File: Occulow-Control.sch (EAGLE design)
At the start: 41 parts, among them T1 DMP3010LK3, T2 DMP3010LK3, T3 DMP3010LK3

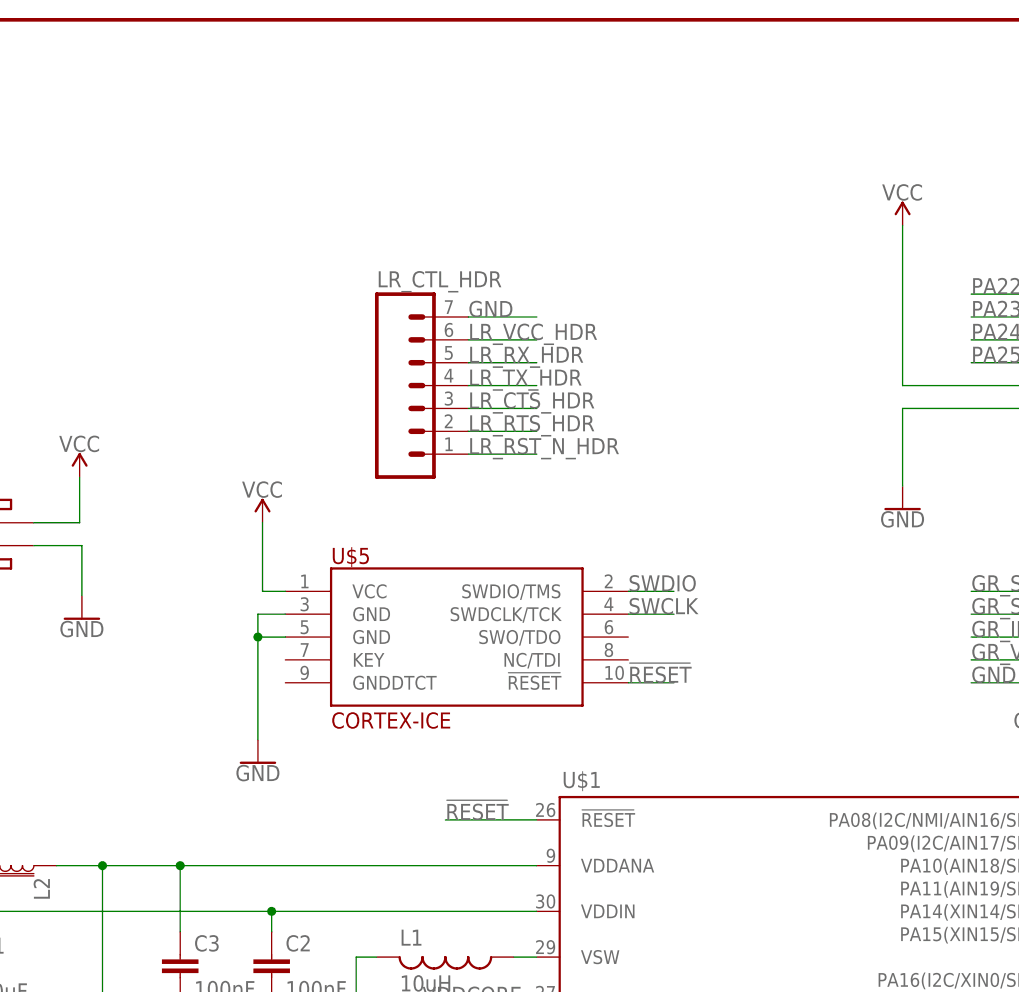
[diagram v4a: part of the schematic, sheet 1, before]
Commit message: Added vcc pull up for reset and button switch. Fixes #7
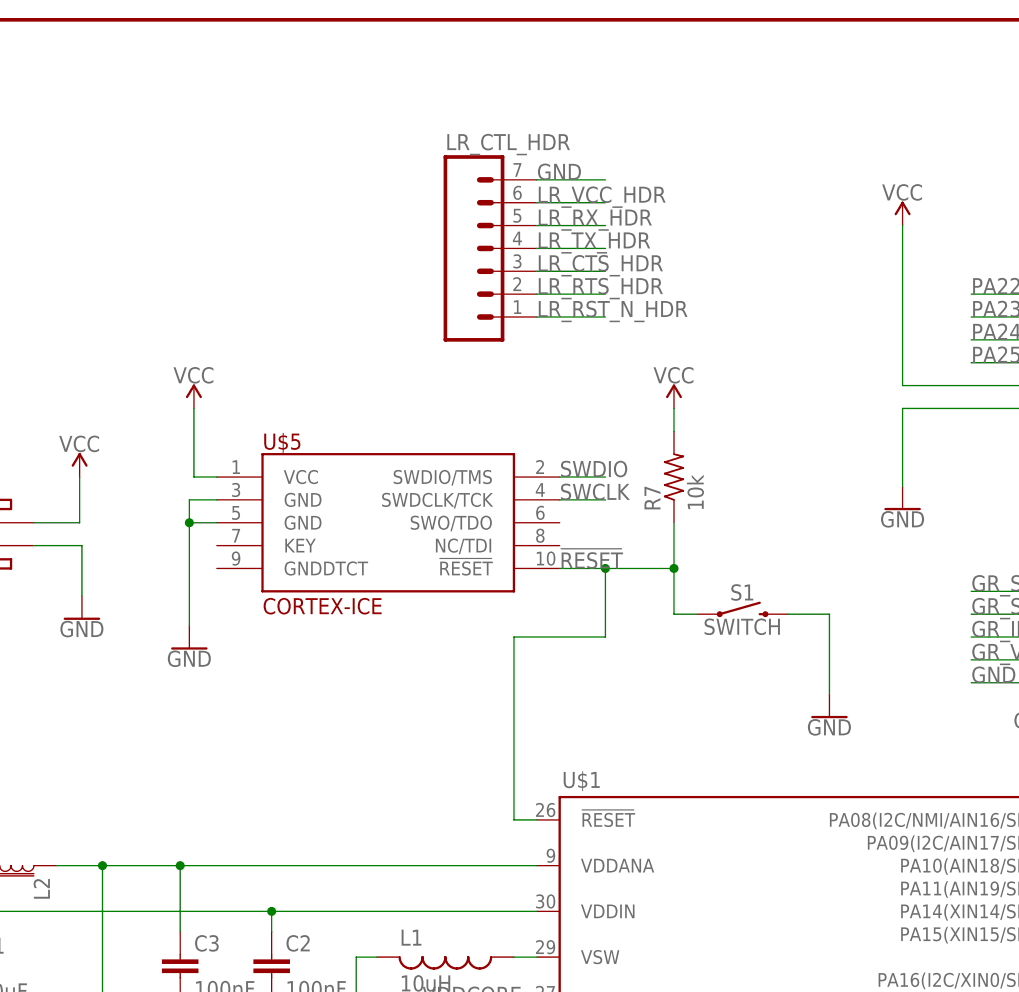
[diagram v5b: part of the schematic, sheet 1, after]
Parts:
- added R7: 10k, resistor:R-US_R1206
- added S1: SWITCH, SparkFun-Switches:MOMENTARY-SWITCH-SPST-SMD-5.2-REDUNDANT
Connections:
- net !RESET: now also R7.1, S1.1
- net GND: now also S1.2
- net VCC: now also R7.2
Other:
- moved on the sheet: LR_CTL_HDR, U$5
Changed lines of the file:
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@@
 <part name="R6" library="resistor" deviceset="R-US_" device="R1206" value="330"/>
 <part name="GND5" library="SparkFun-PowerSymbols" deviceset="GND" device=""/>
+<part name="S1" library="SparkFun-Switches" deviceset="MOMENTARY-SWITCH-SPST" device="-SMD-5.2-REDUNDANT" value="SWITCH"/>
+<part name="R7" library="resistor" deviceset="R-US_" device="R1206" value="10k"/>
+<part name="SUPPLY2" library="SparkFun-PowerSymbols" deviceset="VCC" device=""/>
+<part name="GND6" library="SparkFun-PowerSymbols" deviceset="GND" device=""/>
 </parts>
 <sheets>
@@
 <instance part="T3" gate="G$1" x="226.822" y="134.62"/>
 <instance part="R1" gate="G$1" x="165.1" y="53.34" rot="R90"/>
-<instance part="SUPPLY4" gate="G$1" x="45.72" y="129.54"/>
-<instance part="GND9" gate="1" x="45.212" y="102.87"/>
+<instance part="SUPPLY4" gate="G$1" x="38.1" y="142.24"/>
+<instance part="GND9" gate="1" x="37.592" y="115.57"/>
 <instance part="SUPPLY5" gate="G$1" x="116.84" y="162.56"/>
 <instance part="GND10" gate="1" x="116.84" y="131.064"/>
@@
 <instance part="H2" gate="G$1" x="40.64" y="5.08"/>
 <instance part="H3" gate="G$1" x="45.72" y="5.08"/>
-<instance part="LR_CTL_HDR" gate="G$1" x="63.5" y="142.24"/>
-<instance part="U$5" gate="G$1" x="66.04" y="116.84"/>
+<instance part="LR_CTL_HDR" gate="G$1" x="71.12" y="157.48"/>
+<instance part="U$5" gate="G$1" x="58.42" y="129.54"/>
 <instance part="D1" gate="G$1" x="195.58" y="68.58"/>
 <instance part="R6" gate="G$1" x="195.58" y="55.88" rot="R90"/>
 <instance part="GND5" gate="1" x="195.58" y="43.18"/>
+<instance part="S1" gate="G$1" x="99.06" y="119.38"/>
+<instance part="R7" gate="G$1" x="91.44" y="134.62" rot="R90"/>
+<instance part="SUPPLY2" gate="G$1" x="91.44" y="142.24"/>
+<instance part="GND6" gate="1" x="108.712" y="107.95"/>
 </instances>
 <busses>
@@
 <segment>
 <pinref part="GND9" gate="1" pin="GND"/>
-<wire x1="48.26" y1="119.38" x2="45.212" y2="119.38" width="0.1524" layer="91"/>
-<wire x1="45.212" y1="119.38" x2="45.212" y2="116.84" width="0.1524" layer="91"/>
-<wire x1="45.212" y1="116.84" x2="45.212" y2="105.41" width="0.1524" layer="91"/>
-<wire x1="48.26" y1="116.84" x2="45.212" y2="116.84" width="0.1524" layer="91"/>
-<junction x="45.212" y="116.84"/>
+<wire x1="40.64" y1="132.08" x2="37.592" y2="132.08" width="0.1524" layer="91"/>
+<wire x1="37.592" y1="132.08" x2="37.592" y2="129.54" width="0.1524" layer="91"/>
+<wire x1="37.592" y1="129.54" x2="37.592" y2="118.11" width="0.1524" layer="91"/>
+<wire x1="40.64" y1="129.54" x2="37.592" y2="129.54" width="0.1524" layer="91"/>
+<junction x="37.592" y="129.54"/>
 <pinref part="U$5" gate="G$1" pin="GND@3"/>
 <pinref part="U$5" gate="G$1" pin="GND@5"/>
@@
 <segment>
 <pinref part="LR_CTL_HDR" gate="G$1" pin="7"/>
-<wire x1="68.58" y1="152.4" x2="76.2" y2="152.4" width="0.1524" layer="91"/>
-<label x="68.58" y="152.4" size="1.778" layer="95"/>
+<wire x1="76.2" y1="167.64" x2="83.82" y2="167.64" width="0.1524" layer="91"/>
+<label x="76.2" y="167.64" size="1.778" layer="95"/>
 </segment>
 <segment>
@@
 <wire x1="195.58" y1="45.72" x2="195.58" y2="50.8" width="0.1524" layer="91"/>
 </segment>
+<segment>
+<pinref part="S1" gate="G$1" pin="2"/>
+<pinref part="GND6" gate="1" pin="GND"/>
+<wire x1="104.14" y1="119.38" x2="108.712" y2="119.38" width="0.1524" layer="91"/>
+<wire x1="108.712" y1="119.38" x2="108.712" y2="110.49" width="0.1524" layer="91"/>
+</segment>
 </net>
 <net name="VCC" class="0">
 <segment>
 <pinref part="SUPPLY4" gate="G$1" pin="VCC"/>
-<wire x1="48.26" y1="121.92" x2="45.72" y2="121.92" width="0.1524" layer="91"/>
-<wire x1="45.72" y1="121.92" x2="45.72" y2="129.54" width="0.1524" layer="91"/>
+<wire x1="40.64" y1="134.62" x2="38.1" y2="134.62" width="0.1524" layer="91"/>
+<wire x1="38.1" y1="134.62" x2="38.1" y2="142.24" width="0.1524" layer="91"/>
 <pinref part="U$5" gate="G$1" pin="VCC"/>
 </segment>
@@
 <wire x1="116.84" y1="144.78" x2="116.84" y2="162.56" width="0.1524" layer="91"/>
 </segment>
+<segment>
+<pinref part="R7" gate="G$1" pin="2"/>
+<pinref part="SUPPLY2" gate="G$1" pin="VCC"/>
+<wire x1="91.44" y1="139.7" x2="91.44" y2="142.24" width="0.1524" layer="91"/>
+</segment>
 </net>
 <net name="LR_VCC_CTL" class="0">
@@
 </segment>
 <segment>
-<wire x1="86.36" y1="119.38" x2="91.44" y2="119.38" width="0.1524" layer="91"/>
-<label x="86.36" y="119.38" size="1.778" layer="95"/>
+<wire x1="78.74" y1="132.08" x2="83.82" y2="132.08" width="0.1524" layer="91"/>
+<label x="78.74" y="132.08" size="1.778" layer="95"/>
 <pinref part="U$5" gate="G$1" pin="SWDCLK/TCK"/>
 </segment>
@@
 <net name="SWDIO" class="0">
 <segment>
-<wire x1="86.36" y1="121.92" x2="91.44" y2="121.92" width="0.1524" layer="91"/>
-<label x="86.36" y="121.92" size="1.778" layer="95"/>
+<wire x1="78.74" y1="134.62" x2="83.82" y2="134.62" width="0.1524" layer="91"/>
+<label x="78.74" y="134.62" size="1.778" layer="95"/>
 <pinref part="U$5" gate="G$1" pin="SWDIO/TMS"/>
 </segment>
@@
 <segment>
 <pinref part="U$1" gate="G$1" pin="!RESET"/>
-<wire x1="76.2" y1="96.52" x2="66.04" y2="96.52" width="0.1524" layer="91"/>
-<label x="66.04" y="96.52" size="1.778" layer="95"/>
-</segment>
-<segment>
-<wire x1="86.36" y1="111.76" x2="91.44" y2="111.76" width="0.1524" layer="91"/>
-<label x="86.36" y="111.76" size="1.778" layer="95"/>
+<wire x1="76.2" y1="96.52" x2="73.66" y2="96.52" width="0.1524" layer="91"/>
+<wire x1="73.66" y1="96.52" x2="73.66" y2="116.84" width="0.1524" layer="91"/>
+<wire x1="78.74" y1="124.46" x2="83.82" y2="124.46" width="0.1524" layer="91"/>
+<label x="78.74" y="124.46" size="1.778" layer="95"/>
 <pinref part="U$5" gate="G$1" pin="!RESET"/>
+<wire x1="73.66" y1="116.84" x2="83.82" y2="116.84" width="0.1524" layer="91"/>
+<wire x1="83.82" y1="116.84" x2="83.82" y2="124.46" width="0.1524" layer="91"/>
+<wire x1="83.82" y1="124.46" x2="91.44" y2="124.46" width="0.1524" layer="91"/>
+<junction x="83.82" y="124.46"/>
+<pinref part="S1" gate="G$1" pin="1"/>
+<wire x1="91.44" y1="119.38" x2="93.98" y2="119.38" width="0.1524" layer="91"/>
+<wire x1="91.44" y1="124.46" x2="91.44" y2="119.38" width="0.1524" layer="91"/>
+<pinref part="R7" gate="G$1" pin="1"/>
+<wire x1="91.44" y1="124.46" x2="91.44" y2="129.54" width="0.1524" layer="91"/>
+<junction x="91.44" y="124.46"/>
 </segment>
 </net>
@@
 <segment>
 <pinref part="LR_CTL_HDR" gate="G$1" pin="5"/>
-<wire x1="68.58" y1="147.32" x2="76.2" y2="147.32" width="0.1524" layer="91"/>
-<label x="68.58" y="147.32" size="1.778" layer="95"/>
+<wire x1="76.2" y1="162.56" x2="83.82" y2="162.56" width="0.1524" layer="91"/>
+<label x="76.2" y="162.56" size="1.778" layer="95"/>
 </segment>
 </net>
@@
 <segment>
 <pinref part="LR_CTL_HDR" gate="G$1" pin="4"/>
-<wire x1="68.58" y1="144.78" x2="76.2" y2="144.78" width="0.1524" layer="91"/>
-<label x="68.58" y="144.78" size="1.778" layer="95"/>
+<wire x1="76.2" y1="160.02" x2="83.82" y2="160.02" width="0.1524" layer="91"/>
+<label x="76.2" y="160.02" size="1.778" layer="95"/>
 </segment>
 </net>
@@
 <segment>
 <pinref part="LR_CTL_HDR" gate="G$1" pin="3"/>
-<wire x1="68.58" y1="142.24" x2="76.2" y2="142.24" width="0.1524" layer="91"/>
-<label x="68.58" y="142.24" size="1.778" layer="95"/>
+<wire x1="76.2" y1="157.48" x2="83.82" y2="157.48" width="0.1524" layer="91"/>
+<label x="76.2" y="157.48" size="1.778" layer="95"/>
 </segment>
 </net>
@@
 <segment>
 <pinref part="LR_CTL_HDR" gate="G$1" pin="2"/>
-<wire x1="68.58" y1="139.7" x2="76.2" y2="139.7" width="0.1524" layer="91"/>
-<label x="68.58" y="139.7" size="1.778" layer="95"/>
+<wire x1="76.2" y1="154.94" x2="83.82" y2="154.94" width="0.1524" layer="91"/>
+<label x="76.2" y="154.94" size="1.778" layer="95"/>
 </segment>
 </net>
@@
 <segment>
 <pinref part="LR_CTL_HDR" gate="G$1" pin="1"/>
-<wire x1="68.58" y1="137.16" x2="76.2" y2="137.16" width="0.1524" layer="91"/>
-<label x="68.58" y="137.16" size="1.778" layer="95"/>
+<wire x1="76.2" y1="152.4" x2="83.82" y2="152.4" width="0.1524" layer="91"/>
+<label x="76.2" y="152.4" size="1.778" layer="95"/>
 </segment>
 </net>
@@
 <segment>
 <pinref part="LR_CTL_HDR" gate="G$1" pin="6"/>
-<wire x1="68.58" y1="149.86" x2="76.2" y2="149.86" width="0.1524" layer="91"/>
-<label x="68.58" y="149.86" size="1.778" layer="95"/>
-</segment>
-</net>
+<wire x1="76.2" y1="165.1" x2="83.82" y2="165.1" width="0.1524" layer="91"/>
+<label x="76.2" y="165.1" size="1.778" layer="95"/>
+</segment>
+</net>
